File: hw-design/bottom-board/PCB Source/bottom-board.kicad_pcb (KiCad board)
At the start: 4 copper layers, 172 x 140.5 mm, 388 parts, among them J1 Power Jack, J10 NYS215, J11 USB_B, J12 USB_A, J13 DIN_5, J14 DIN_5, J16 NYS215, J17 NYS215, J18 MJ-3536N, J2 HMI_POWER, J3 AS0A823-H4SB-7H, J4 RJ45, J5 HMI_DATA, J6 SERIAL_DEBUG, J7 NYS215, J8 NYS215, J9 NYS215, K1 G6S-2, K2 G6S-2, Q1 2N7002, Q10 J110, Q11 J110, Q12 2N7002, Q13 2N7002, Q14 J110, Q15 J110, Q16 2N7002, Q17 J110, Q2 2N7002, Q3 2N7002, Q4 2N7002, Q8 J110, Q9 2N7002, U1 TL750M10CKVURG3, U10 LM358, U11 OPA1678, U12 OPA1678, U13 DG9426E, U14 LM4811, U15 LM2596S-5, U16 TPS2041B, U17 6N136S, U18 ISL83086E, U2 LD1117S50TR, U20 ADC122S021, U21 MIC2076A, U22 74LVC3G17, U24 MCP4922-EP, U4 LD1117S50TR_SOT223, U5 AP2120N-3.3, U6 CS4265, U7 AT24CS08, U8 LM4562, U9 DG9426E, X1 24.576MHz

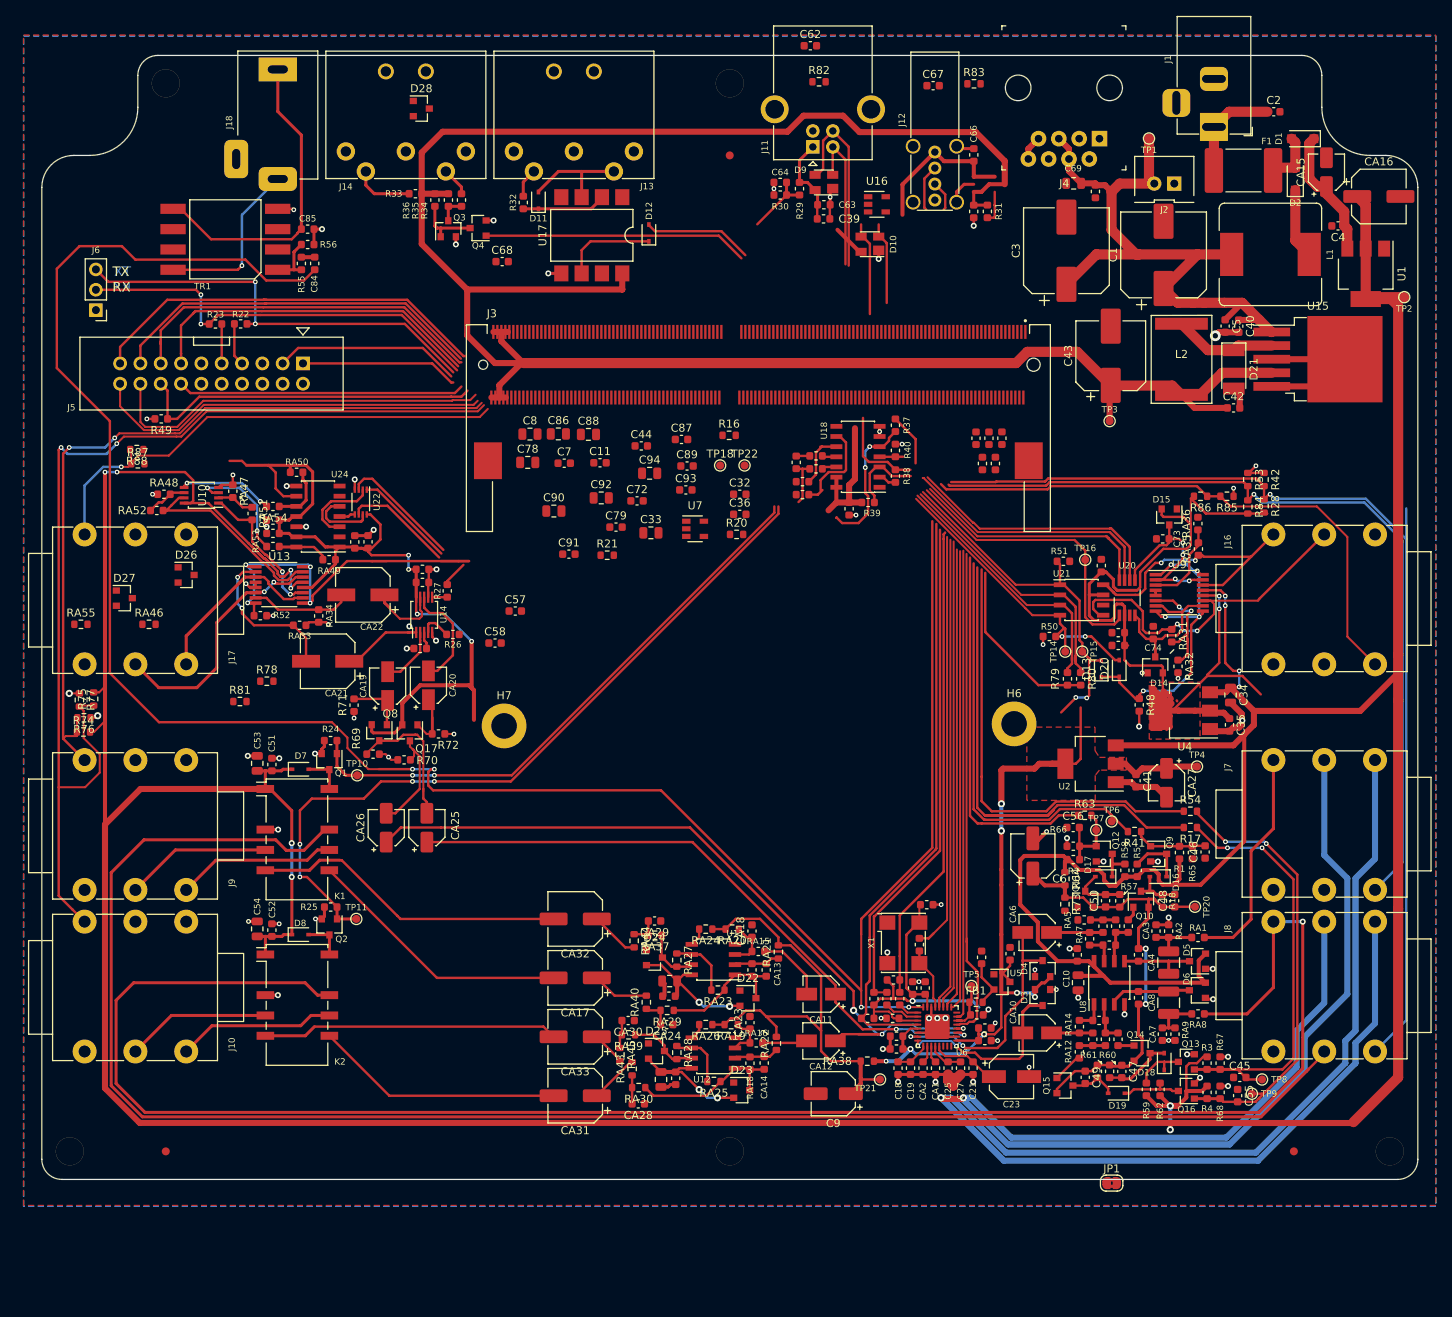
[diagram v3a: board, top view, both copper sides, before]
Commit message: first half of star ground
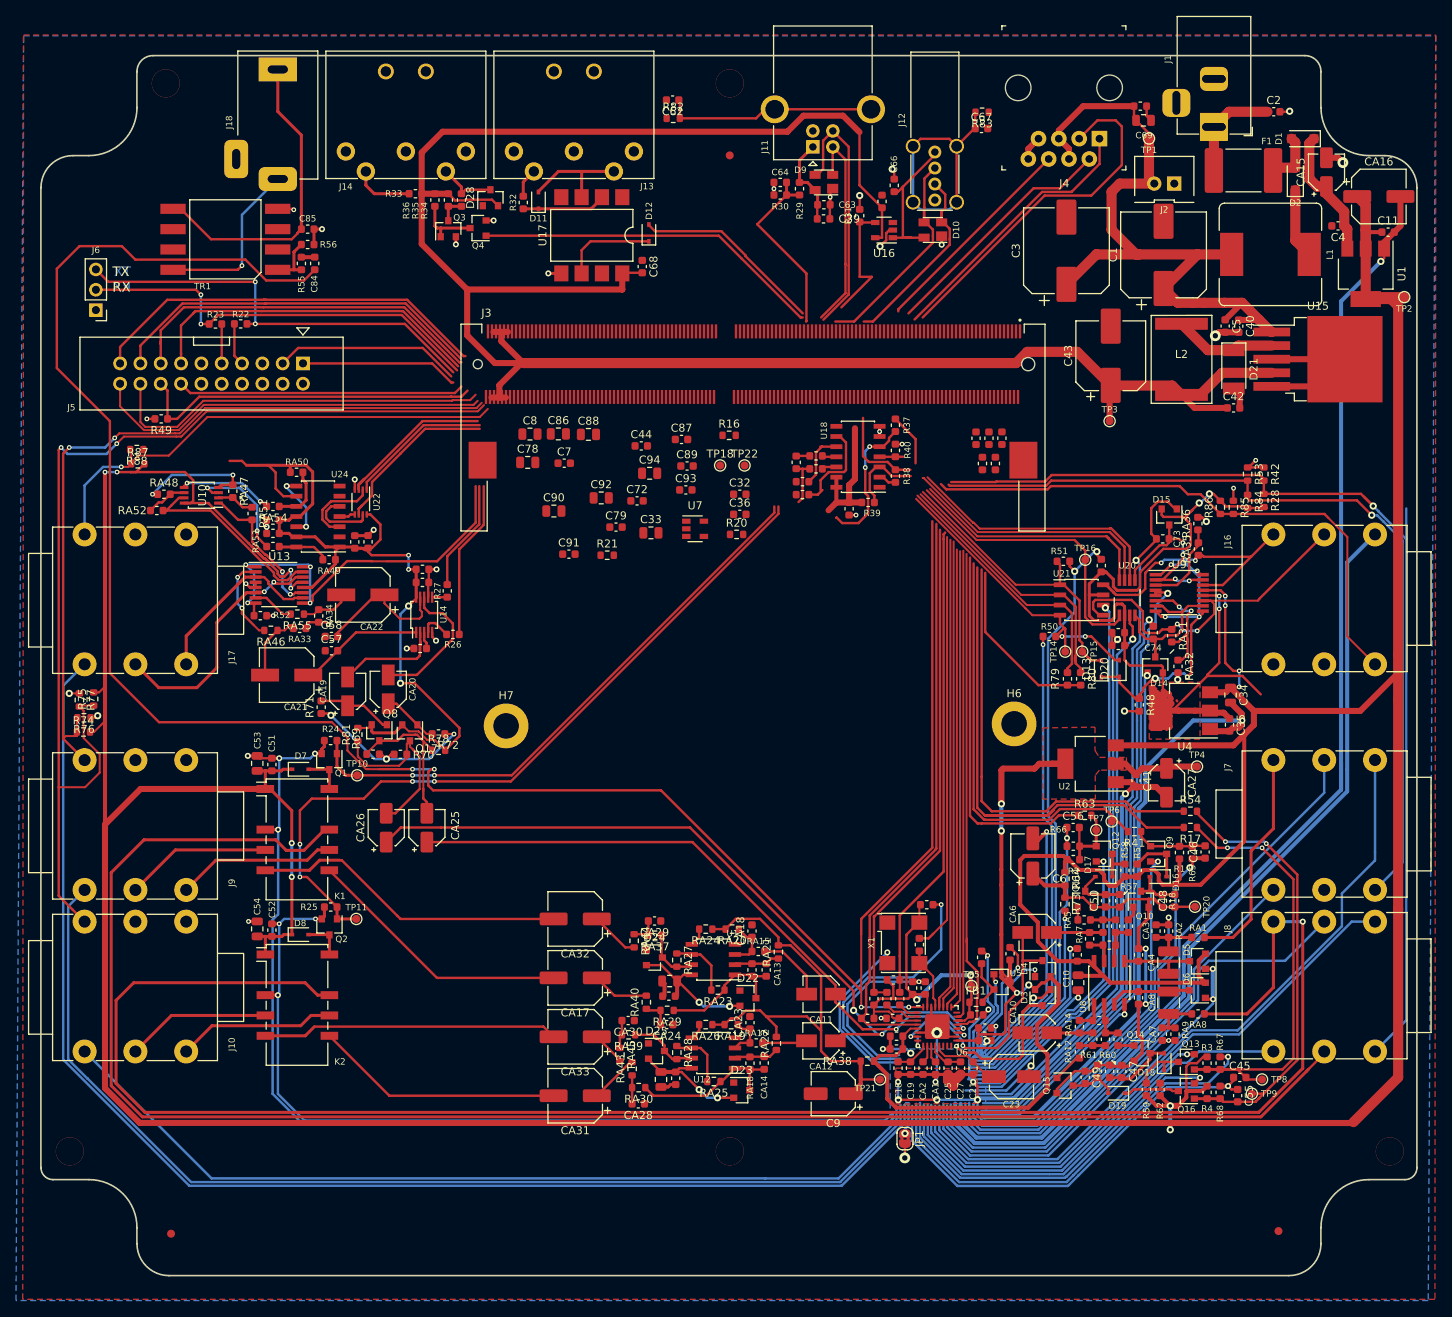
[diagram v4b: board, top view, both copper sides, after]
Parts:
- removed D26, D27: BAT54S, Package_TO_SOT_SMD:SOT-23
- moved C11 102.6 mm to (228.4, 41.7)
- moved RA55 27.1 mm to (92.0, 89.4), turned to 180 degrees
- moved JP1 26.4 mm to (168.0, 155.0), turned to 270 degrees
- moved C57 23.5 mm to (96.3, 94.0)
- moved R78 23.1 mm to (109.7, 106.4)
- moved C58 20.5 mm to (96.3, 92.2)
- moved R82 18.8 mm to (139.0, 27.4)
- moved C62 18.5 mm to (138.9, 25.1), turned to 180 degrees
- moved C68 17.5 mm to (135.1, 46.0), turned to 270 degrees
- moved R31 16.0 mm to (162.3, 39.6), turned to 270 degrees
- moved R81 15.3 mm to (99.6, 104.5), turned to 90 degrees
- moved RA46 15.3 mm to (88.7, 91.4), turned to 180 degrees
- moved D28 14.1 mm to (116.1, 37.4), turned to 90 degrees
- moved C70 12.1 mm to (197.4, 25.9), turned to 0 degrees
- moved C69 11.8 mm to (197.8, 27.7), turned to 0 degrees
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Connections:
- D28 pad 2: +10V -> +5VD
- R48 pad 2: GNDA -> GNDD
- R52 pad 2: GNDA -> GNDD
- RA32 pad 2: GNDA -> GNDD
- RA36 pad 2: GNDA -> GNDD
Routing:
- net GNDA: track 455.9 -> 3025.4 mm, vias 62 -> 75
- net RS485_RX+: track 6.03 -> 50.2 mm
- net RS485_TX+: track 0.00 -> 34.3 mm
- net RS485_TX-: track 0.00 -> 30.6 mm
- net Net-(C67-Pad1): track 3.84 -> 32.1 mm
- net RS485_RX-: track 1.67 -> 28.5 mm
- net Net-(C62-Pad1): track 0.00 -> 26.7 mm
- net HP_CLOCK: track 0.00 -> 19.8 mm
- net +5VA: track 217.2 -> 236.6 mm, vias 11 -> 8
- net USB_HOST_DRV: track 0.00 -> 15.7 mm
- net USB_DEV_DET: track 8.37 -> 23.1 mm
- net GNDD: track 61.3 -> 75.2 mm, vias 18 -> 27
- net HP_UP/DN: track 3.30 -> 14.4 mm
- net USB_HOST_DP: track 14.1 -> 25.1 mm
- net MIDI_UART_TX: track 33.1 -> 43.8 mm
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- added copper zone on B.Cu, net GNDA
- added copper zone on F.Cu, net GNDA
- removed copper zone on B.Cu, net (none)
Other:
- board size 172 x 140.5 mm -> 172 x 152.5 mm
- board text added: "Enclosure [0mm clearance]"
- board text added: "Heatsink [5.41mm clearance]"

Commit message: route codec to new SoM
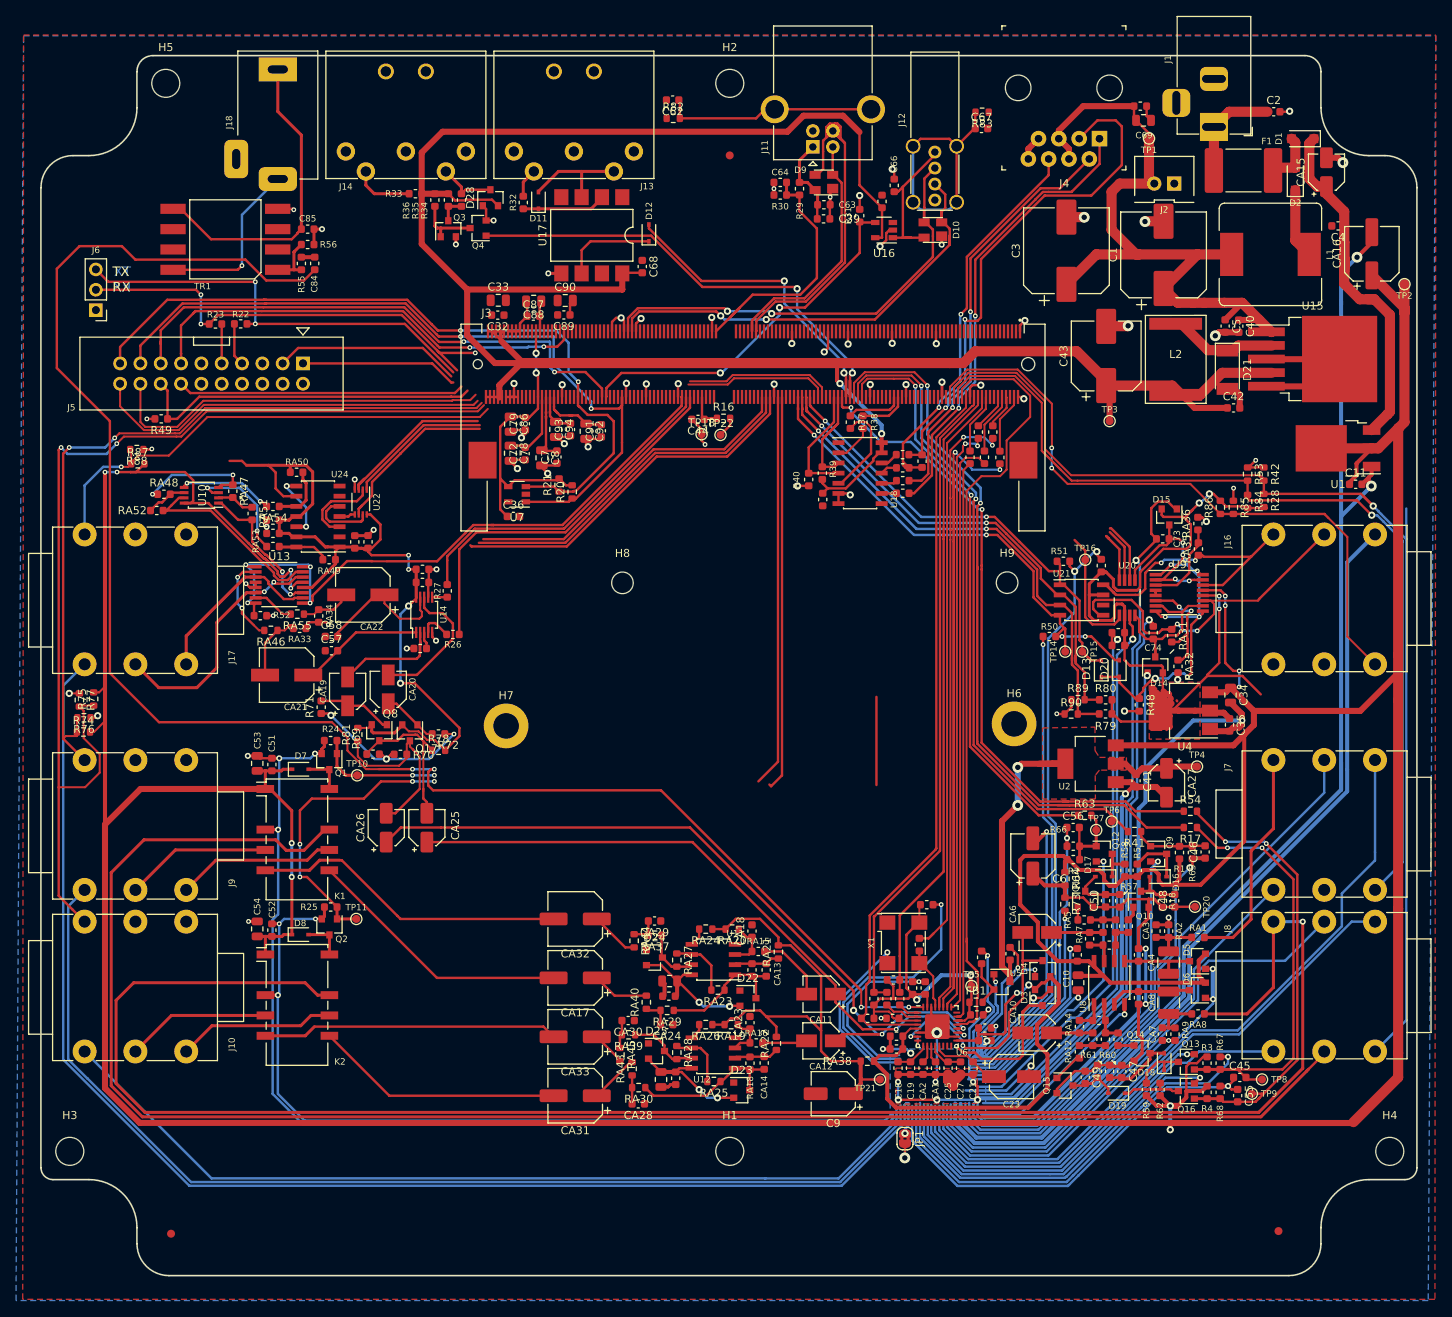
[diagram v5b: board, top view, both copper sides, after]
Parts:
- added H8: HOLE, MountingHole:MountingHole_2.7mm, F.Cu at (132.7, 85.5)
- added H9: HOLE, MountingHole:MountingHole_2.7mm, F.Cu at (180.7, 85.5)
- added R89: 15K, Resistor_SMD:R_0603_1608Metric, F.Cu at (189.6, 100.1)
- added R90: 15K, Resistor_SMD:R_0603_1608Metric, F.Cu at (188.7, 101.9)
- H1, H2, H3, H4, H5: footprint footprints:Hole_3.5mm -> MountingHole:MountingHole_3.5mm
- U1: footprint Package_TO_SOT_SMD:SOT-223-3_TabPin2 -> Package_TO_SOT_SMD:TO-252-3_TabPin2
- moved C32 37.6 mm to (117.1, 52.0), turned to 180 degrees
- moved C33 34.8 mm to (117.1, 50.2)
- moved C11 31.8 mm to (224.3, 73.2)
- moved C36 28.3 mm to (119.0, 77.2)
- moved C90 26.4 mm to (125.5, 50.2)
- moved C89 24.4 mm to (125.3, 52.0), turned to 180 degrees
- moved C87 24.1 mm to (121.5, 52.2)
- moved U7 22.7 mm to (119.5, 74.4), turned to 180 degrees
- moved U1 22.1 mm to (222.1, 68.7), turned to 180 degrees
- moved R20 21.2 mm to (126.4, 74.1), turned to 90 degrees
- moved C88 18.0 mm to (121.6, 50.3), turned to 180 degrees
- moved C79 17.2 mm to (120.5, 65.6), turned to 90 degrees
- moved C93 16.3 mm to (126.1, 66.3), turned to 90 degrees
- moved C91 15.9 mm to (130.0, 66.5), turned to 90 degrees
- moved R47 15.7 mm to (170.1, 70.3), turned to 270 degrees
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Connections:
- C77 pad 1: GNDA -> GNDD
- J3 pad 106: EXP_EN2 -> EXP_EN1
- J3 pad 108: EXP_FLAG2 -> EXP_FLAG1
- J3 pad 110: EXP_FLAG1 -> EXP_FLAG2
- J3 pad 112: EXP_EN1 -> EXP_EN2
- J3 pad 126: (no net) -> OUT1_DETECT
- J3 pad 128: (no net) -> OUT2_DETECT
- J3 pad 130: (no net) -> CV_OUT_DET
- J3 pad 196: PM_LEDS_OE -> (no net)
- J3 pad 202: (no net) -> PM_LEDS_OE
- J3 pad 68: OUT1_DETECT -> (no net)
- J3 pad 70: OUT2_DETECT -> (no net)
- J3 pad 72: CV_OUT_DET -> (no net)
- R50 pad 2: GNDA -> GNDD
- R51 pad 2: GNDA -> GNDD
- R79 pad 2: +3V0 -> +5VP
- R80 pad 2: +3V0 -> +5VP
- U13 pad 4: GNDA -> GNDD
- U13 pad 5: GNDA -> GNDD
- U21 pad 6: GNDA -> GNDD
- U9 pad 4: GNDA -> GNDD
- U9 pad 5: GNDA -> GNDD
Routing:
- net GNDA: track 3025.4 -> 2803.7 mm, vias 75 -> 71
- net GNDD: track 75.2 -> 235.5 mm, vias 27 -> 60
- net Net-(R14-Pad1): track 58.7 -> 141.4 mm, vias 0 -> 2
- net CODEC_SPDIF_OUT: track 275.0 -> 212.7 mm
- net PM_LEDS_SCL: track 47.3 -> 95.3 mm, vias 0 -> 2
- net OUT1_DETECT: track 98.0 -> 144.5 mm
- net OUT2_DETECT: track 133.7 -> 178.3 mm
- net CV_OUT_DET: track 62.4 -> 105.7 mm
- net PM_LEDS_SDA: track 50.9 -> 94.2 mm, vias 0 -> 2
- net +3V3: track 0.00 -> 37.3 mm, vias 0 -> 2
- net CODEC_MUTEC: track 62.0 -> 97.3 mm
- net Net-(C4-Pad1): track 16.6 -> 50.0 mm
- net USB_HOST_DP: track 25.1 -> 57.5 mm, vias 0 -> 2
- net EXP_FLAG2: track 33.4 -> 64.3 mm, vias 0 -> 2
- net USB_HOST_DRV: track 15.7 -> 46.2 mm, vias 0 -> 2
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
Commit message: finish routing SoM
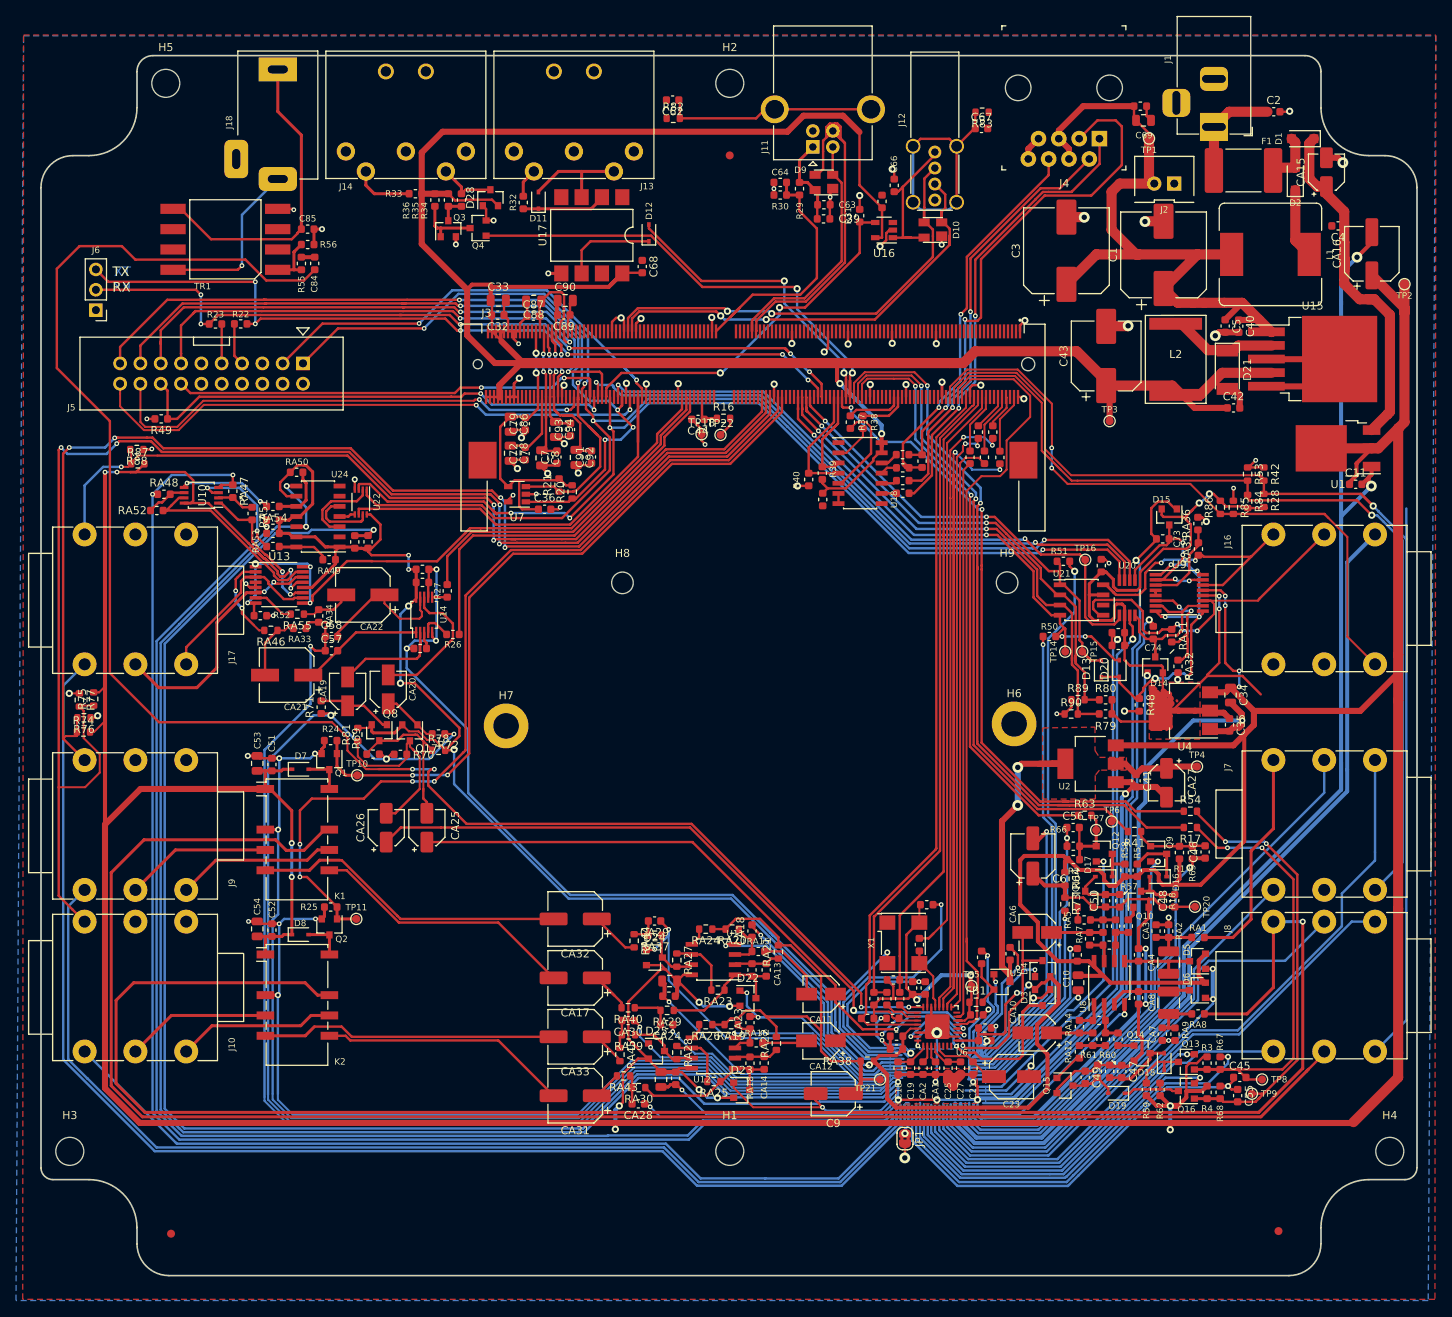
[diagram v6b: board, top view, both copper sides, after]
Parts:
- moved C36 4.00 mm to (122.9, 76.3)
- moved C92 3.50 mm to (126.9, 69.8)
- moved C91 3.50 mm to (128.8, 69.8)
- moved RA40 2.37 mm to (133.4, 138.6), turned to 180 degrees
- moved RA43 1.39 mm to (132.8, 147.1), turned to 180 degrees
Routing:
- net GNDA: track 2803.7 -> 4263.2 mm, vias 71 -> 86
- net CV_ADC_DIN: track 25.7 -> 125.0 mm, vias 0 -> 2
- net CV_ADC_SCLK: track 27.0 -> 123.3 mm, vias 0 -> 4
- net CV_ADC_DOUT: track 6.77 -> 79.8 mm, vias 0 -> 2
- net CV_ADC_~CS~: track 15.6 -> 81.6 mm, vias 0 -> 2
- net +5VA: track 242.3 -> 307.9 mm, vias 8 -> 10
- net HMI_RFU_02(TX): track 23.3 -> 58.3 mm, vias 0 -> 2
- net CV_DAC_~CS~: track 21.5 -> 53.1 mm
- net CLI_UART_TX: track 72.3 -> 102.2 mm, vias 2 -> 6
- net HMI_RFU_01(RX): track 19.8 -> 49.2 mm, vias 0 -> 2
- net +10V: track 683.0 -> 709.6 mm, vias 16 -> 18
- net IN2_TBP: track 85.8 -> 112.0 mm
- net IN1_TBP: track 65.5 -> 91.5 mm
- net CLI_UART_RX: track 75.8 -> 101.5 mm, vias 3 -> 6
- net HMI_UART_RX: track 50.3 -> 71.5 mm, vias 0 -> 2
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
